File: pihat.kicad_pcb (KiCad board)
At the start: 2 copper layers, 65 x 56.5 mm, 5 parts, among them J1 Raspberry_Pi_2_3

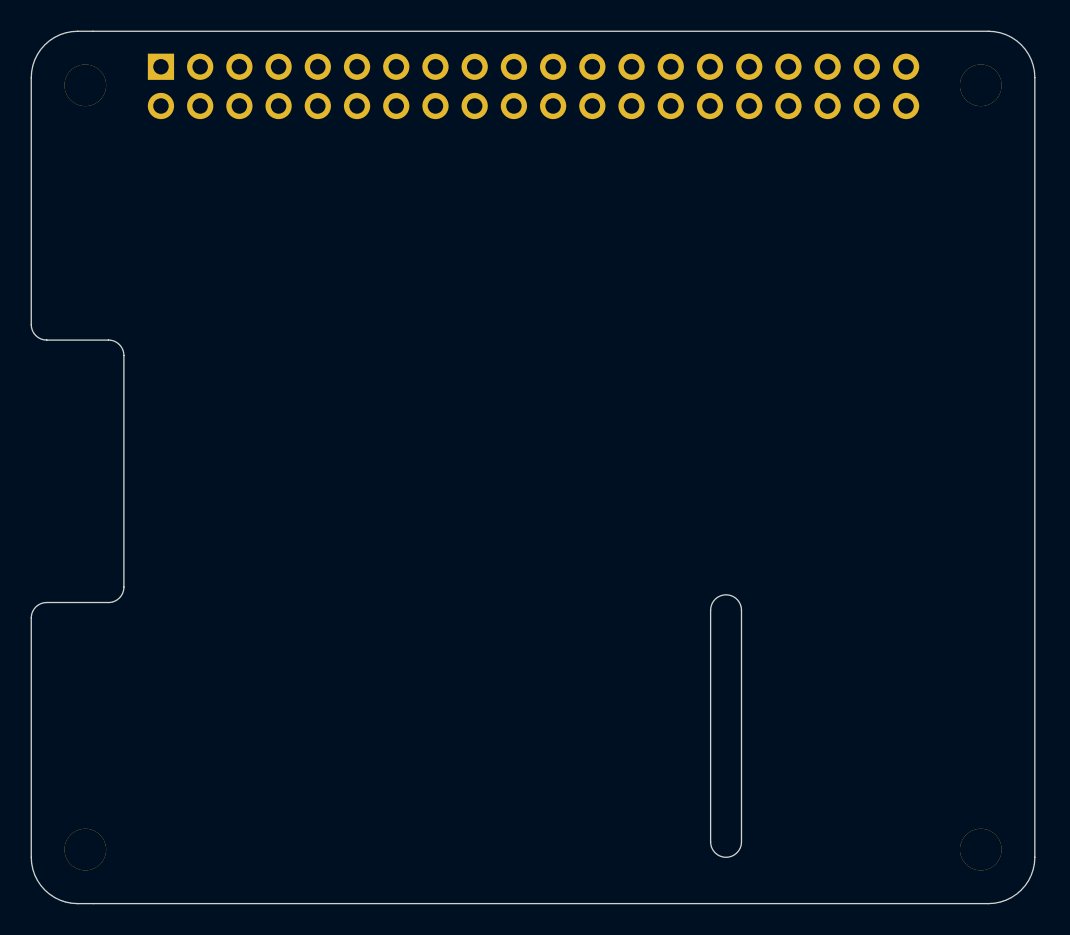
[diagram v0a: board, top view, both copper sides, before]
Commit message: Add initial schematic for hat
This adds a USB<->UART converter and a 1-wire bus master, as well as
screw connectors for heating elements and sensors.
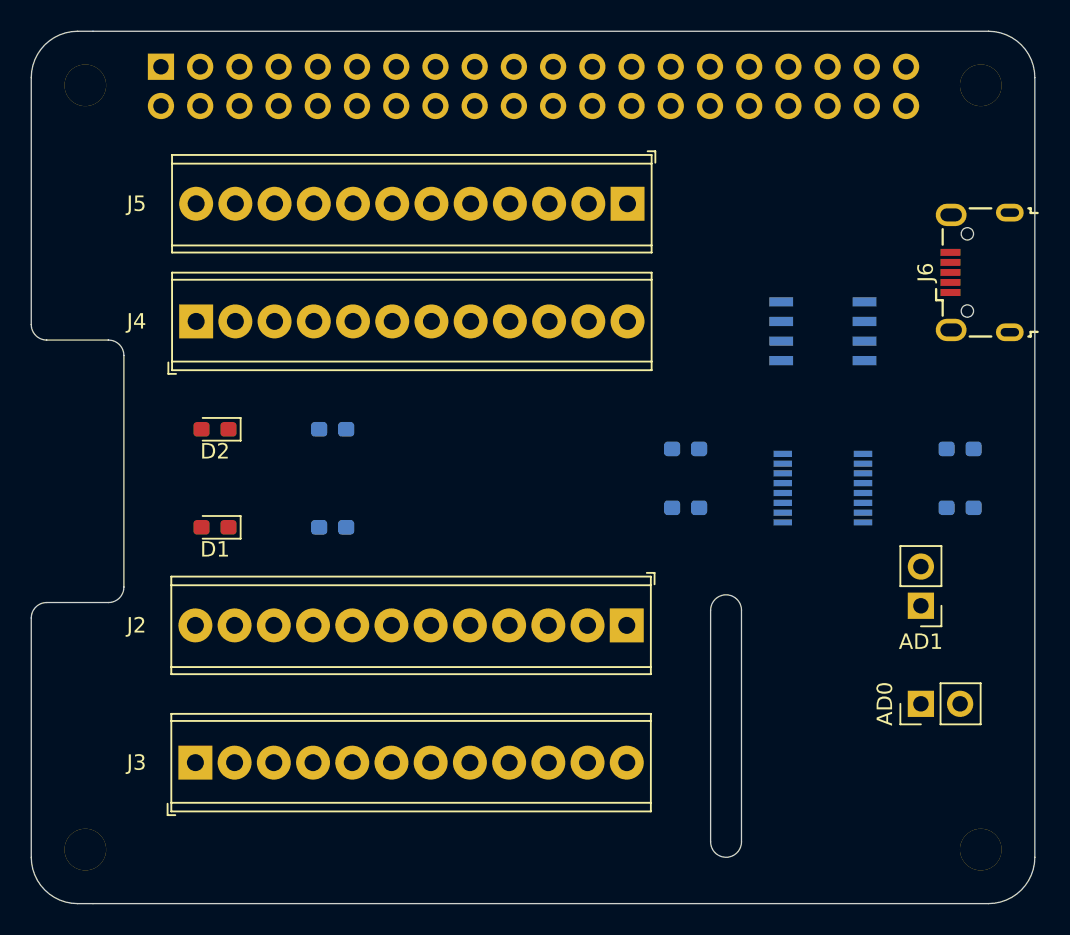
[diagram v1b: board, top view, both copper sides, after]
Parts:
- added AD0: Jumper, Connector_PinHeader_2.54mm:PinHeader_1x02_P2.54mm_Vertical, F.Cu at (134.6, 99.1)
- added AD1: Jumper, Connector_PinHeader_2.54mm:PinHeader_1x02_P2.54mm_Vertical, F.Cu at (134.6, 92.7)
- added C1: C, Capacitor_SMD:C_0603_1608Metric_Pad1.05x0.95mm_HandSolder, B.Cu at (137.2, 86.4)
- added C2: C, Capacitor_SMD:C_0603_1608Metric_Pad1.05x0.95mm_HandSolder, B.Cu at (119.4, 86.4)
- added D1: LED, LED_SMD:LED_0603_1608Metric_Pad1.05x0.95mm_HandSolder, F.Cu at (88.9, 87.6)
- added D2: LED, LED_SMD:LED_0603_1608Metric_Pad1.05x0.95mm_HandSolder, F.Cu at (88.9, 81.3)
- added J2: Screw_Terminal_01x12, TerminalBlock_Phoenix:TerminalBlock_Phoenix_MPT-0,5-12-2.54_1x12_P2.54mm_Horizontal, F.Cu at (115.6, 94.0)
- added J3: Screw_Terminal_01x12, TerminalBlock_Phoenix:TerminalBlock_Phoenix_MPT-0,5-12-2.54_1x12_P2.54mm_Horizontal, F.Cu at (87.6, 102.9)
- added J4: Screw_Terminal_01x12, TerminalBlock_Phoenix:TerminalBlock_Phoenix_MPT-0,5-12-2.54_1x12_P2.54mm_Horizontal, F.Cu at (87.7, 74.3)
- added J5: Screw_Terminal_01x12, TerminalBlock_Phoenix:TerminalBlock_Phoenix_MPT-0,5-12-2.54_1x12_P2.54mm_Horizontal, F.Cu at (115.6, 66.7)
- added J6: USB_B_Micro, Connector_USB:USB_Micro-B_Wuerth_629105150521, F.Cu at (138.4, 71.1)
- added R1: R, Resistor_SMD:R_0603_1608Metric_Pad1.05x0.95mm_HandSolder, B.Cu at (137.2, 82.5)
- added R2: R27, Resistor_SMD:R_0603_1608Metric_Pad1.05x0.95mm_HandSolder, B.Cu at (119.4, 82.5)
- added R3: R270, Resistor_SMD:R_0603_1608Metric_Pad1.05x0.95mm_HandSolder, B.Cu at (96.5, 87.6)
- added R4: R270, Resistor_SMD:R_0603_1608Metric_Pad1.05x0.95mm_HandSolder, B.Cu at (96.5, 81.3)
- added U1: DS2482-100, Package_SO:SOIC-8_3.9x4.9mm_P1.27mm, B.Cu at (128.3, 74.9)
- added U2: FT230XS, Package_SO:SSOP-16_3.9x4.9mm_P0.635mm, B.Cu at (128.3, 85.1)
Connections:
- J1 pad 10: Net-(J1-Pad10) -> /UART_RXD
- J1 pad 11: Net-(J1-Pad11) -> /HEATER_1
- J1 pad 3: Net-(J1-Pad3) -> /I2C_SDA
- J1 pad 5: Net-(J1-Pad5) -> /I2C_SCL
- J1 pad 8: Net-(J1-Pad8) -> /UART_TXD
